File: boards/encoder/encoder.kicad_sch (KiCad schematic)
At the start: 31 parts, among them J1 Conn_PWR, J2 BLS, J3 SWD, J4 Sensore, SW1 SW_SPST, SW2 SW_SPST, SW3 SW_Push, U1 TPS62A02A, U2 MSPM0G310x

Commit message: v0.1.14
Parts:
- removed J2: BLS, symbol Connector_Generic:Conn_01x04
- added J3: Sensore, symbol Connector_Generic:Conn_01x04
- added RV1: R_Potentiometer, symbol Device:R_Potentiometer
- C2: renamed from C1; value 0.1u -> 100u
- C3: renamed from C2; value 10u -> 4.7u
- C4: renamed from C3; value 0.1u -> 22u
- C5: renamed from C4; value 470n -> C
- C6: renamed from C7; value 0.1u -> C
- C7: renamed from C8; value 10u -> C
- R1: renamed from R8; value 200k -> R
- R10: renamed from R5; value 100k -> R
- R2: renamed from R9; value 10k -> R
- R3: renamed from R1; value 200 -> R
- R4: renamed from R2; value 200 -> R
- R5: renamed from R6; value 500 -> R
- R6: renamed from R7; value 500 -> R
- R7: renamed from R10; value 500 -> R
- R8: renamed from R3; value 500 -> R
- R9: renamed from R4; value 500 -> R
- renumbered C6 to C1, C5 to C8, D2 to D1, D3 to D2, D1 to D3, J3 to J2, U2 to U1, U1 to U2
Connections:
- net AY_RX: now also J4.4 (Pin_4), U1.17 (PA13); no longer J4.3 (Pin_3)
- net AY_TX: now also J4.3 (Pin_3), U1.18 (PA14_CLK_OUT_A0_12); no longer J4.4 (Pin_4)
- net CAN_RX: now also U1.31 (PA27_RTC_OUT_A0_0)
- net CAN_STB: now also U1.8 (PA4_LFCLK_IN_LFXOUT)
- net CAN_TX: now also U1.30 (PA26_A0_1)
- net COS_IN: now also U1.28 (PA24_A0_3); no longer U1.31 (PA27_RTC_OUT_A0_0)
- net GND: now also J3.4 (Pin_4)
- net PEN: no longer U2.4 (EN)
- net RS485_RX: now also U1.13 (PA9_RTC_OUT_CLK_OUT)
- net RS485_TX: now also U1.12 (PA8)
- net VBIAS: now also U1.20 (PA16_A1_1_FCC_IN); no longer U1.30 (PA26_A0_1)
- net VDD: now also J3.1 (Pin_1)
- net at C1.2, R1.2: now also RV1.1; no longer R2.1, U2.5 (FB)
- net PWR_SW: now reaches L1.1, U2.2 (SW)
- net BSL_UART_RX renamed UART_RX
- net UART_RX: now also J3.3 (Pin_3)
- net BSL_UART_TX renamed UART_TX
- net UART_TX: now also J3.2 (Pin_2)
- new net: R2.1, RV1.3
- new net PWR_EN: U2.4 (EN)
- new net PWR_FB: RV1.2, U2.5 (FB)
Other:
- moved on the sheet: C1, C2, C3, C4, C5, C6, C7, C8, D1, D2, D3, J1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

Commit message: v0.1.16
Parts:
- C5: value C -> 470n
- C6: value C -> 10u
- C7: value C -> 100n
- R1: value R -> 455k
- R10: value R -> 100k
- R2: value R -> 90k
- R3, R4: value R -> 75
- R5, R6: value R -> 47k
- R7: value R -> 499k
- R8: value R -> 200
- R9: value R -> 100
- RV1: value R_Potentiometer -> 10k
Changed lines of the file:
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@@
 			)
 		)
-		(property "Value" "R"
+		(property "Value" "455k"
 			(at 154.686 30.734 0)
 			(effects
@@
 			)
 		)
-		(property "Value" "C"
+		(property "Value" "100n"
 			(at 148.336 127 0)
 			(effects
@@
 			)
 		)
-		(property "Value" "R"
+		(property "Value" "47k"
 			(at 43.18 74.93 0)
 			(effects
@@
 			)
 		)
-		(property "Value" "R"
+		(property "Value" "75"
 			(at 128.27 76.2 0)
 			(effects
@@
 			)
 		)
-		(property "Value" "R"
+		(property "Value" "499k"
 			(at 57.15 74.93 0)
 			(effects
@@
 			)
 		)
-		(property "Value" "R"
+		(property "Value" "47k"
 			(at 26.67 74.93 0)
 			(effects
@@
 			)
 		)
-		(property "Value" "R_Potentiometer"
+		(property "Value" "10k"
 			(at 154.94 40.6399 0)
 			(effects
@@
 			)
 		)
-		(property "Value" "C"
+		(property "Value" "10u"
 			(at 136.652 126.746 0)
 			(effects
@@
 			)
 		)
-		(property "Value" "C"
+		(property "Value" "470n"
 			(at 158.75 126.9999 0)
 			(effects
@@
 			)
 		)
-		(property "Value" "R"
+		(property "Value" "90k"
 			(at 154.94 49.5299 0)
 			(effects
@@
 			)
 		)
-		(property "Value" "R"
+		(property "Value" "100"
 			(at 97.79 86.36 0)
 			(effects
@@
 			)
 		)
-		(property "Value" "R"
+		(property "Value" "200"
 			(at 86.36 86.36 0)
 			(effects
@@
 			)
 		)
-		(property "Value" "R"
+		(property "Value" "100k"
 			(at 168.91 126.9999 0)
 			(effects
@@
 			)
 		)
-		(property "Value" "R"
+		(property "Value" "75"
 			(at 138.43 76.2 0)
 			(effects

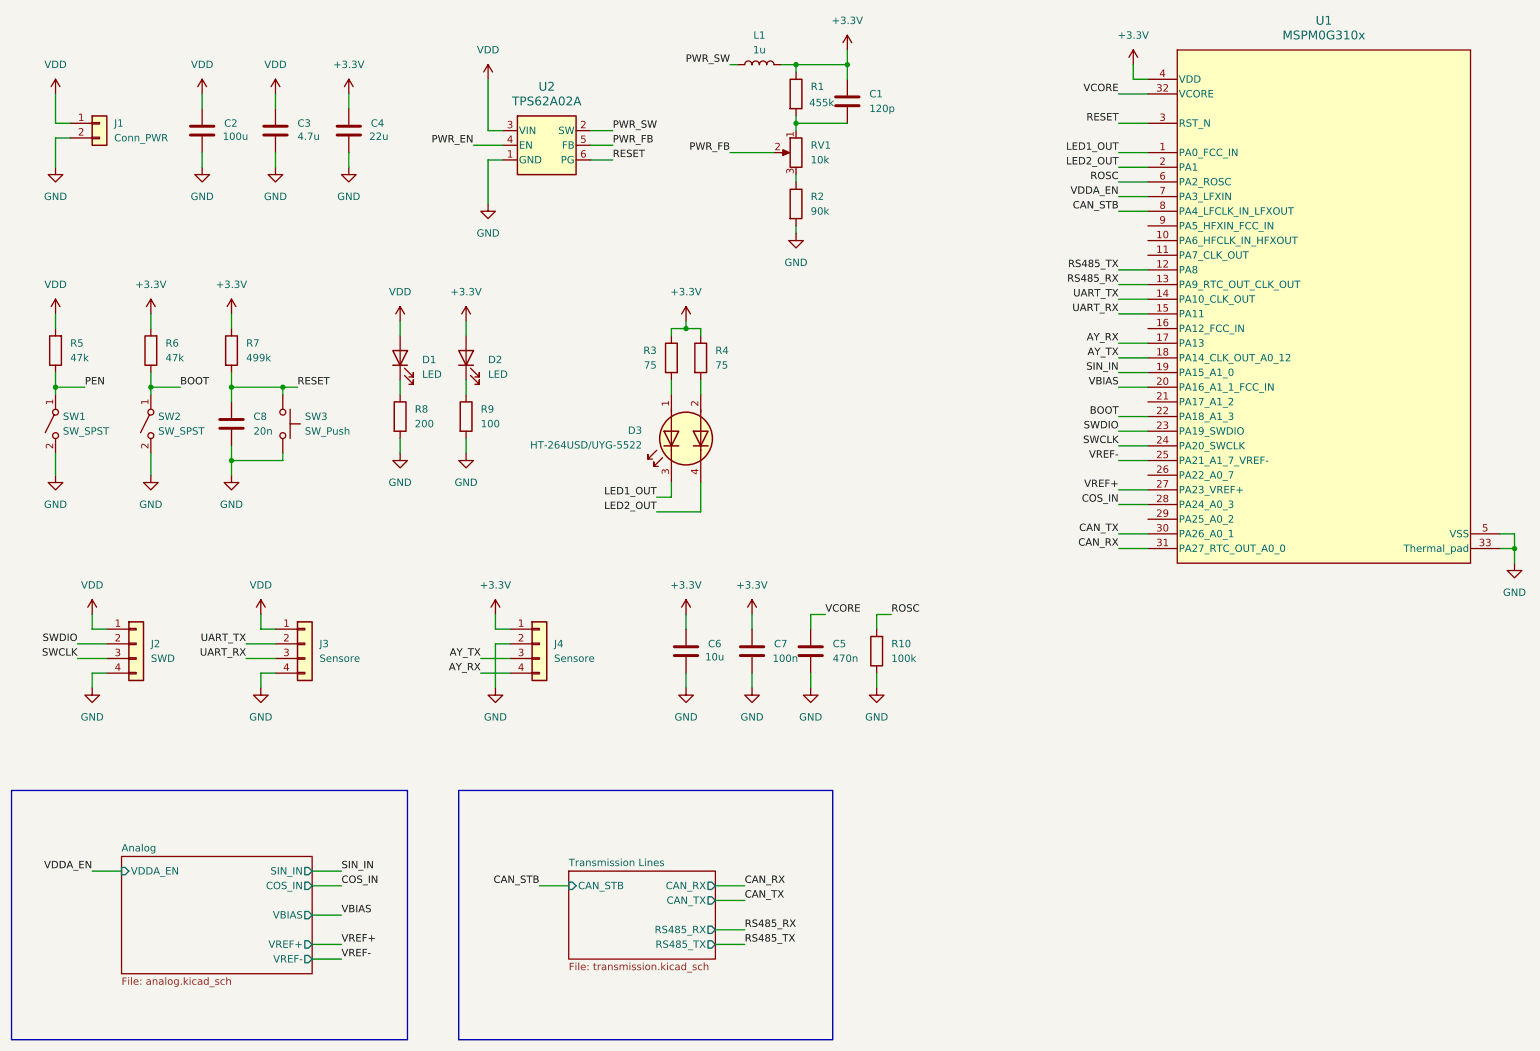
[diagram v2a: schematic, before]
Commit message: Added EEPROM
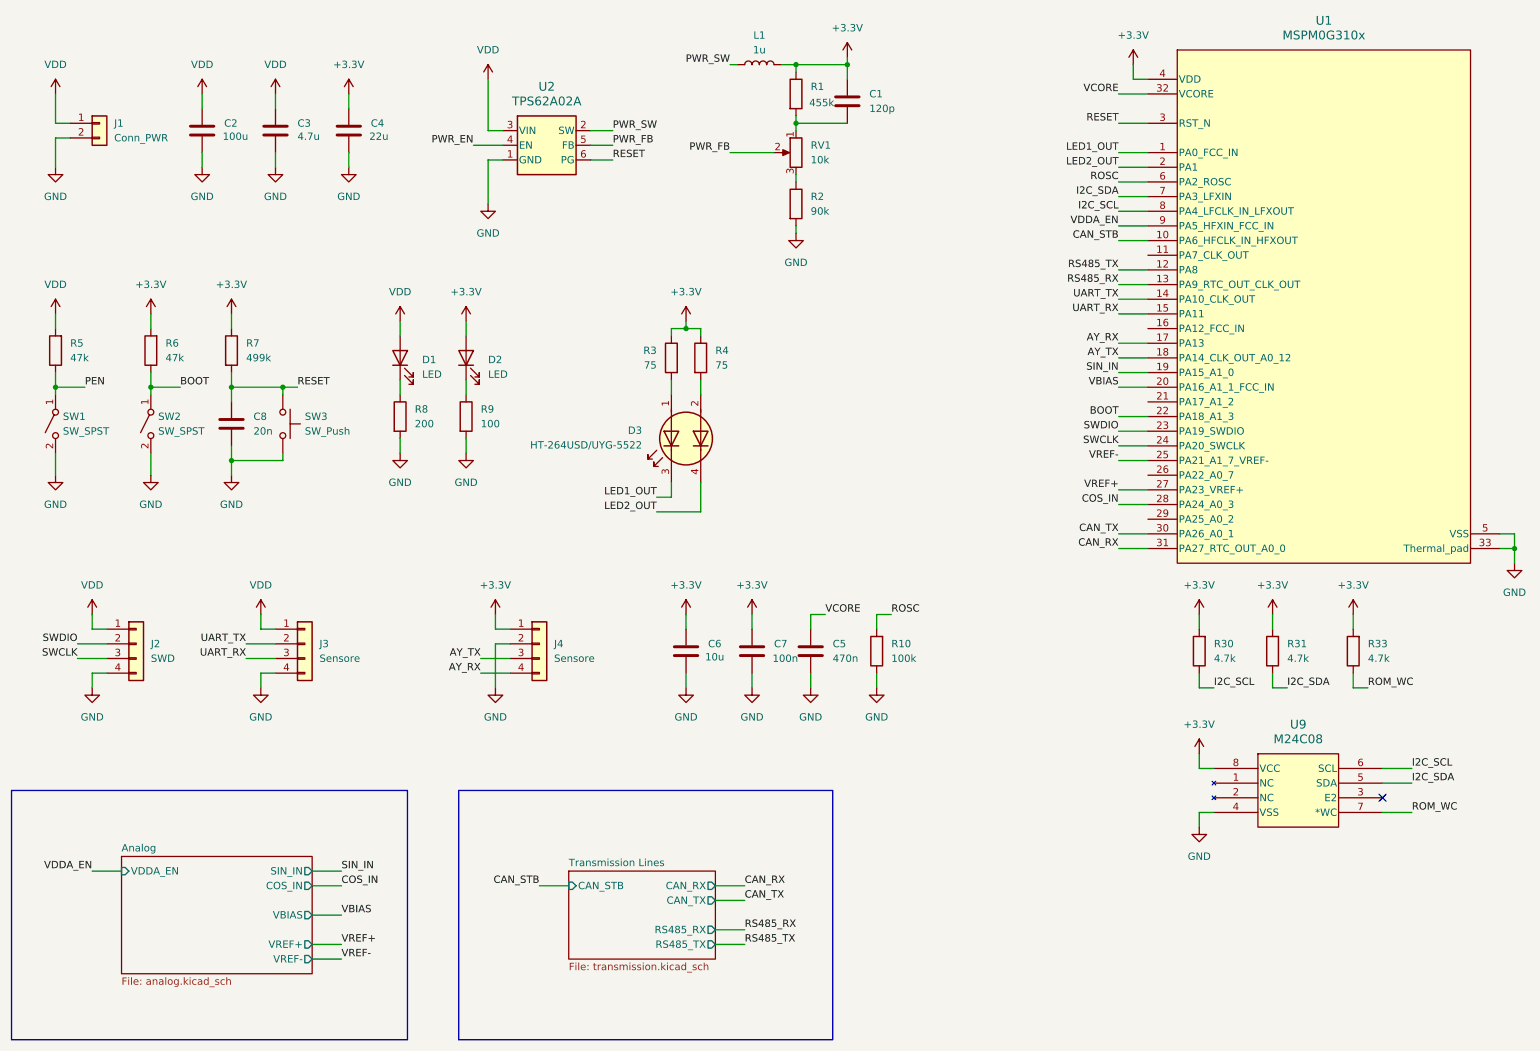
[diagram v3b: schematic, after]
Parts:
- added R30, R31, R33: 4.7k, symbol Device:R
- added U9: M24C08, SO8N_4X5X1P27_STM, symbol Memory_EEPROM:M24C08
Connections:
- net +3.3V: now also R30.2, R31.2, R33.2, U9.8 (VCC)
- net CAN_STB: now also U1.10 (PA6_HFCLK_IN_HFXOUT); no longer U1.8 (PA4_LFCLK_IN_LFXOUT)
- net GND: now also U9.4 (VSS)
- net VDDA_EN: now also U1.9 (PA5_HFXIN_FCC_IN); no longer U1.7 (PA3_LFXIN)
- new net I2C_SCL: R30.1, U1.8 (PA4_LFCLK_IN_LFXOUT), U9.6 (SCL)
- new net I2C_SDA: R31.1, U1.7 (PA3_LFXIN), U9.5 (SDA)
- new net ROM_WC: R33.1, U9.7 (*WC)
- no-connect marks 0 -> 1

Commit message: v0.1.17
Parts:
- removed C1: 120p, symbol Device:C
- removed C2: 100u, symbol Device:C
- removed C3: 4.7u, symbol Device:C
- removed C4: 22u, symbol Device:C
- removed J1: Conn_PWR, symbol Connector_Generic:Conn_01x02
- removed L1: 1u, symbol Device:L
- removed R1: 455k, symbol Device:R
- removed R2: 90k, symbol Device:R
- removed RV1: 10k, symbol Device:R_Potentiometer
- removed U2: TPS62A02A, SOT6_DRL_TEX, symbol Regulator_Switching:TPS62A02A
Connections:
- net PEN is gone; now on net PWR_EN: R5.1, SW1.1 (A)
- net GND: now also U9.3 (E2)
- net LED1_OUT: now also D3.4 (K2); no longer D3.3 (K1)
- net LED2_OUT: now also D3.3 (K1); no longer D3.4 (K2)
- net at D3.1 (A1): now also R4.2; no longer R3.2
- net at D3.2 (A2): now also R3.2; no longer R4.2
- no-connect marks 1 -> 0
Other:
- added sheet PSU (psu.kicad_sch)
- note added: "Additional subsheets"
- note added: "EEPROM Memory"
- note added: "General connectors"
- note added: "Human interfaces"
- note added: "MSPM Decoupling components"
- moved on the sheet: C5, C6, C7, C8, D1, D2, D3, J2, J3, J4, R10, R3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

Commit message: v0.1.18
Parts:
- renumbered C6 to C1, C7 to C2, C5 to C3, C8 to C4, J2 to J1, J3 to J2, J4 to J3, R10 to R1, R31 to R10, R33 to R11, R5 to R2, R6 to R3, R7 to R4, R3 to R5, R4 to R6, R8 to R7, R9 to R8, R30 to R9, U9 to U2
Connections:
- no-connect marks 0 -> 5
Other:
- note added: "Microcontroller"
- company: (none) -> MetisVela
- title: (none) -> Wanda
- moved on the sheet: C4, D1, D2, D3, R10, R11, R2, R3, R4, R5, R6, R7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

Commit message: Fixed some values
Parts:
- R5, R6: value 75 -> 65
- R7: value 200 -> 150
- R8: value 100 -> 65
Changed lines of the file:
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@@
 			)
 		)
-		(property "Value" "75"
+		(property "Value" "65"
 			(at 82.55 119.38 0)
 			(effects
@@
 			)
 		)
-		(property "Value" "100"
+		(property "Value" "65"
 			(at 135.89 132.08 0)
 			(effects
@@
 			)
 		)
-		(property "Value" "200"
+		(property "Value" "150"
 			(at 124.46 132.08 0)
 			(effects
@@
 			)
 		)
-		(property "Value" "75"
+		(property "Value" "65"
 			(at 92.71 119.38 0)
 			(effects

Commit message: v0.2.1
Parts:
- C1, C2, C3, C4: footprint (none) -> Capacitor_SMD:C_0603_1608Metric
- D1, D2: footprint (none) -> LED_SMD:LED_0603_1608Metric
- R1, R10, R11, R2, R3, R4, R5, R6, R7, R8, R9: footprint (none) -> Resistor_SMD:R_0603_1608Metric
- SW3: footprint Button_Switch_SMD:SW_MEC_5GSH9 -> (none)
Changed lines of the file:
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@@
 			)
 		)
-		(property "Footprint" ""
+		(property "Footprint" "Capacitor_SMD:C_0603_1608Metric"
 			(at 39.0652 40.64 0)
 			(effects
@@
 			)
 		)
-		(property "Footprint" ""
+		(property "Footprint" "LED_SMD:LED_0603_1608Metric"
 			(at 121.92 120.65 0)
 			(effects
@@
 			)
 		)
-		(property "Footprint" ""
+		(property "Footprint" "Resistor_SMD:R_0603_1608Metric"
 			(at 28.448 176.53 90)
 			(effects
@@
 			)
 		)
-		(property "Footprint" ""
+		(property "Footprint" "LED_SMD:LED_0603_1608Metric"
 			(at 133.35 120.65 0)
 			(effects
@@
 			)
 		)
-		(property "Footprint" ""
+		(property "Footprint" "Resistor_SMD:R_0603_1608Metric"
 			(at 44.958 118.11 90)
 			(effects
@@
 			)
 		)
-		(property "Footprint" ""
+		(property "Footprint" "Resistor_SMD:R_0603_1608Metric"
 			(at 86.868 118.11 90)
 			(effects
@@
 			)
 		)
-		(property "Footprint" ""
+		(property "Footprint" "Resistor_SMD:R_0603_1608Metric"
 			(at 55.372 118.11 90)
 			(effects
@@
 			)
 		)
-		(property "Footprint" ""
+		(property "Footprint" "Resistor_SMD:R_0603_1608Metric"
 			(at 28.448 118.11 90)
 			(effects
@@
 			)
 		)
-		(property "Footprint" "Button_Switch_SMD:SW_MEC_5GSH9"
+		(property "Footprint" ""
 			(at 71.12 130.81 0)
 			(effects
@@
 			)
 		)
-		(property "Footprint" ""
+		(property "Footprint" "Capacitor_SMD:C_0603_1608Metric"
 			(at 58.1152 134.62 0)
 			(effects
@@
 			)
 		)
-		(property "Footprint" ""
+		(property "Footprint" "Capacitor_SMD:C_0603_1608Metric"
 			(at 27.6352 40.64 0)
 			(effects
@@
 			)
 		)
-		(property "Footprint" ""
+		(property "Footprint" "Capacitor_SMD:C_0603_1608Metric"
 			(at 51.7652 40.64 0)
 			(effects
@@
 			)
 		)
-		(property "Footprint" ""
+		(property "Footprint" "Resistor_SMD:R_0603_1608Metric"
 			(at 41.148 176.53 90)
 			(effects
@@
 			)
 		)
-		(property "Footprint" ""
+		(property "Footprint" "Resistor_SMD:R_0603_1608Metric"
 			(at 131.572 130.81 90)
 			(effects
@@
 			)
 		)
-		(property "Footprint" ""
+		(property "Footprint" "Resistor_SMD:R_0603_1608Metric"
 			(at 120.142 130.81 90)
 			(effects
@@
 			)
 		)
-		(property "Footprint" ""
+		(property "Footprint" "Resistor_SMD:R_0603_1608Metric"
 			(at 64.008 36.83 90)
 			(effects
@@
 			)
 		)
-		(property "Footprint" ""
+		(property "Footprint" "Resistor_SMD:R_0603_1608Metric"
 			(at 55.118 176.53 90)
 			(effects
@@
 			)
 		)
-		(property "Footprint" ""
+		(property "Footprint" "Resistor_SMD:R_0603_1608Metric"
 			(at 88.392 118.11 90)
 			(effects

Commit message: Metis-Vela footprint library
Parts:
- U1: footprint RHB0032D-IPC_A -> metis-vela:RHB0032D-IPC_A
- U2: footprint SO8N_4X5X1P27_STM -> metis-vela:SO8N_4X5X1P27_STM
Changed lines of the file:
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@@
 			)
 		)
-		(property "Footprint" "RHB0032D-IPC_A"
+		(property "Footprint" "metis-vela:RHB0032D-IPC_A"
 			(at 207.01 35.56 0)
 			(effects
@@
 			)
 		)
-		(property "Footprint" "SO8N_4X5X1P27_STM"
+		(property "Footprint" "metis-vela:SO8N_4X5X1P27_STM"
 			(at 71.12 170.18 0)
 			(effects
